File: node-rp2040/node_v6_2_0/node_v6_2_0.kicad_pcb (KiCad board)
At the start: 6 copper layers, 45 x 75 mm, 95 parts, among them J1 786463001, J10 Connector, USB-TYPE-C-16P, J11 Barrel_Jack_Switch, J2 U.FL, J3 Conn_Coaxial, J4 Conn_01x10, J5 Conn_01x10, J6 U.FL, J7 Barrel_Jack_Switch, J9 U.FL, Q1 DMG2301L, SW2 PTS636 SM50J SMTR LFS, SW3 PTS636 SM50J SMTR LFS, U1 RP2040, U12 CAT24M01W, U14 W25Q128, U2 USBLC6-2SC6, U3 AP2112K-3.3, U5 MCP73831-2-OT, U6 RFM69HCW, U7 PCF8523T, U8 SP3485EN, U9 SIM7080G, Y1 ABM8-272-T3

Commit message: finished layout v6.2
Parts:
- removed C8: 0.1u, JLCPCB:C_0402
- added C4: 0.1u, JLCPCB:C_0402, F.Cu at (125.2, 46.8)
- R17, R18: footprint JLCPCB:R_0805 -> JLCPCB:R_0603
- moved C48 145.5 mm to (106.6, 33.8), turned to 90 degrees
- moved C30 116.9 mm to (136.0, 50.8), turned to 180 degrees
- moved C47 108.0 mm to (109.1, 34.4)
- moved C9 106.4 mm to (127.5, 51.4)
- moved C25 104.3 mm to (127.5, 57.4)
- moved C44 102.8 mm to (112.9, 56.2)
- moved C17 102.0 mm to (134.9, 61.0), turned to 180 degrees
- moved R15 101.3 mm to (112.8, 53.6), turned to 180 degrees
- moved R4 98.8 mm to (113.2, 38.6), turned to -90 degrees
- moved R14 98.4 mm to (112.8, 54.6), turned to 180 degrees
- moved C28 98.2 mm to (138.2, 70.5), turned to 90 degrees
- moved R3 93.7 mm to (119.4, 29.0), turned to 90 degrees
- moved C13 92.6 mm to (110.8, 46.2), turned to 180 degrees
- moved C16 79.6 mm to (124.4, 58.0), turned to -90 degrees
- moved C15 79.0 mm to (122.2, 59.6), turned to -90 degrees
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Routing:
- net +3.3V: track 38.5 -> 57.8 mm, vias 0 -> 2
- net SDA: track 1.38 -> 15.1 mm, vias 1 -> 2
- net SCL: track 1.37 -> 14.2 mm, vias 1 -> 2
- net TX1: track 0.00 -> 12.4 mm
- net RX1: track 0.00 -> 11.5 mm
- net Net-(BT1-+): track 0.00 -> 10.9 mm
- net /MCU/CS: track 10.6 -> 1.39 mm
- net +1V1: track 9.45 -> 18.5 mm
- net /MCU/D1: track 9.96 -> 2.11 mm
- net /MCU/D3: track 15.3 -> 7.52 mm, vias 2 -> 1
- net /MCU/D0: track 14.3 -> 6.94 mm
- net USB-: track 0.00 -> 7.22 mm
- net /MCU/CLK: track 14.8 -> 8.09 mm, vias 2 -> 1
- net Net-(J10-CC1): track 0.00 -> 6.61 mm
- net 485_!RE: track 0.00 -> 6.55 mm, vias 0 -> 1
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
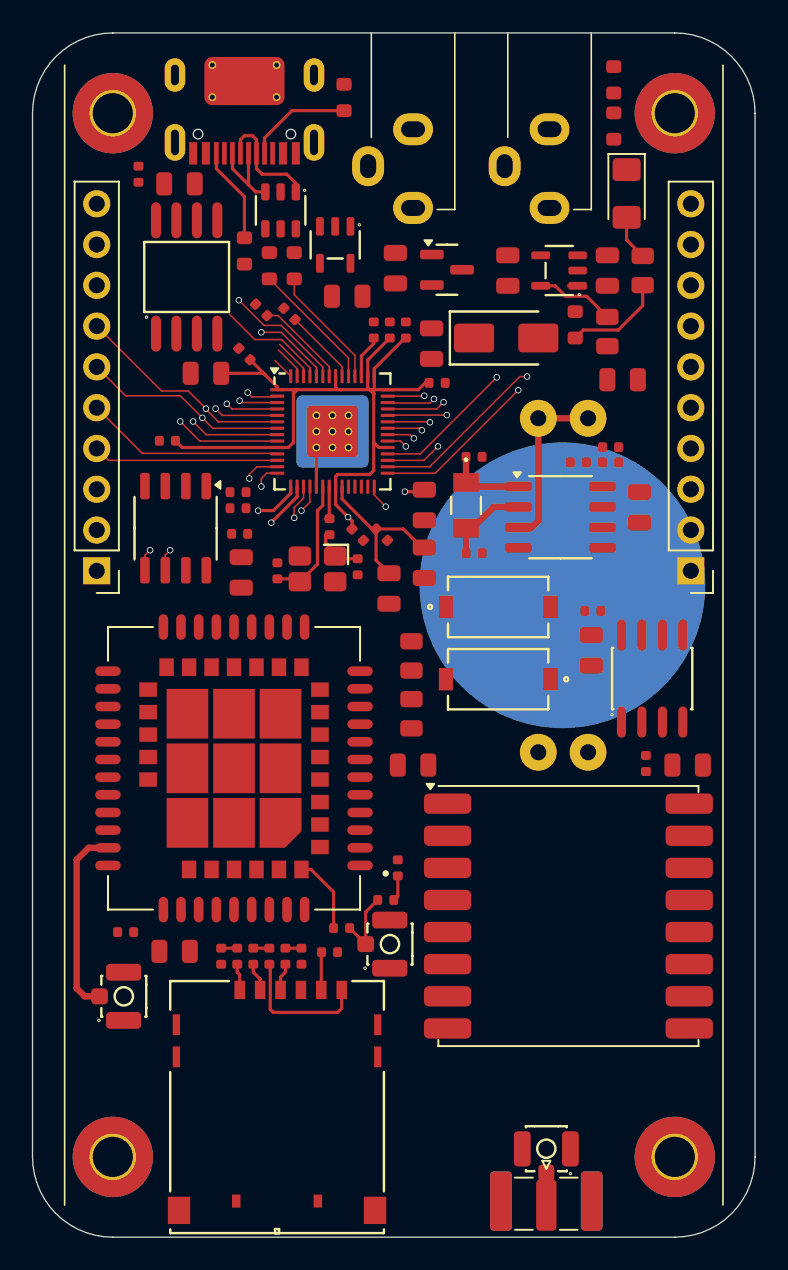
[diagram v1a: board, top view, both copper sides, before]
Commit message: finished routing; todo: labels and silkscreen, final review
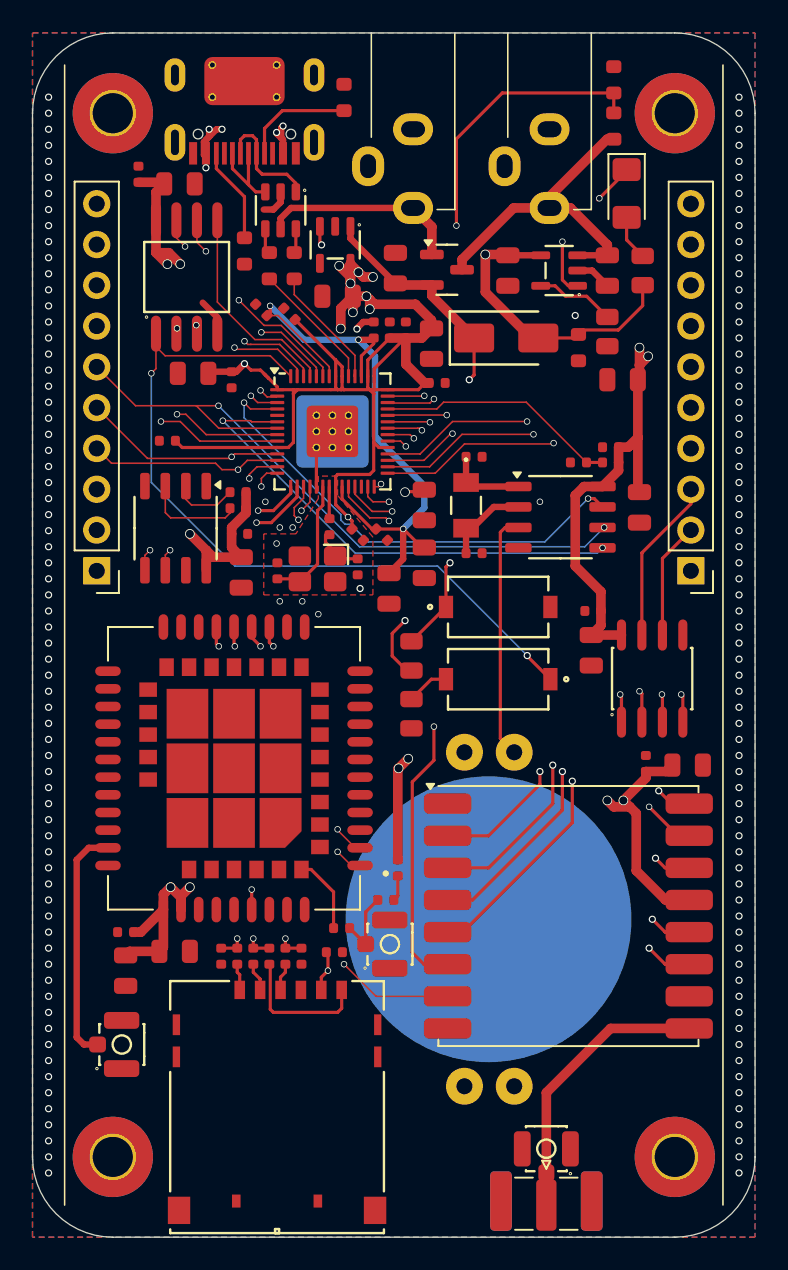
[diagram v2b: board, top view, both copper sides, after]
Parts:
- moved C42 22.0 mm to (105.8, 83.4), turned to -90 degrees
- moved BT1 21.3 mm to (128.4, 80.2)
- moved J6 3.00 mm to (104.8, 88.0)
- moved C5 1.79 mm to (112.4, 46.6), turned to -90 degrees
- moved R8 1.43 mm to (134.0, 44.6), turned to -90 degrees
- moved R14 1.00 mm to (112.8, 53.6)
- moved R15 1.00 mm to (112.8, 54.6)
- moved C13 0.80 mm to (110.0, 46.2)
- moved C40 0.60 mm to (119.0, 41.4)
- moved C37 0.30 mm to (118.8, 82.2)
- turned TH1 to 180 degrees
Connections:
- J6 pad 3: (no net) -> GND
- J9 pad 3: (no net) -> GND
- U1 pad 13: RFM_DIO0 -> RFM_DIO5
- U1 pad 14: RFM_DIO1 -> RFM_DIO3
- U1 pad 34: RFM_DIO2 -> RFM_DIO4
- U1 pad 35: RFM_DIO3 -> RFM_DIO0
- U1 pad 36: RFM_DIO4 -> RFM_DIO1
- U1 pad 37: RFM_DIO5 -> RFM_DIO2
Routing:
- net +3.3V: track 57.8 -> 295.6 mm, vias 2 -> 22
- net VBUS: track 6.31 -> 68.9 mm, vias 0 -> 6
- net MISO: track 0.00 -> 49.0 mm, vias 0 -> 3
- net /MCU/CS: track 1.39 -> 49.3 mm, vias 0 -> 2
- net 485_!RE: track 6.55 -> 50.6 mm, vias 1 -> 4
- net 485_DE: track 5.58 -> 49.3 mm, vias 1 -> 4
- net RFM_DIO3: track 1.73 -> 44.1 mm, vias 1 -> 4
- net SCL: track 14.2 -> 54.1 mm, vias 2 -> 3
- net RFM_DIO5: track 2.64 -> 42.2 mm, vias 1 -> 2
- net RFM_RST: track 3.49 -> 42.5 mm, vias 1 -> 2
- net RFM_DIO4: track 2.18 -> 39.9 mm, vias 1 -> 2
- net SDA: track 15.1 -> 52.2 mm, vias 2 -> 3
- net TX1: track 12.4 -> 49.3 mm, vias 0 -> 2
- net RFM_CS: track 1.54 -> 38.1 mm, vias 1 -> 2
- net +VSW: track 0.00 -> 35.3 mm, vias 0 -> 2
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- added copper zone on B.Cu, net GND
- added copper zone on F.Cu, net GND
- added copper zone on In1.Cu, net GND

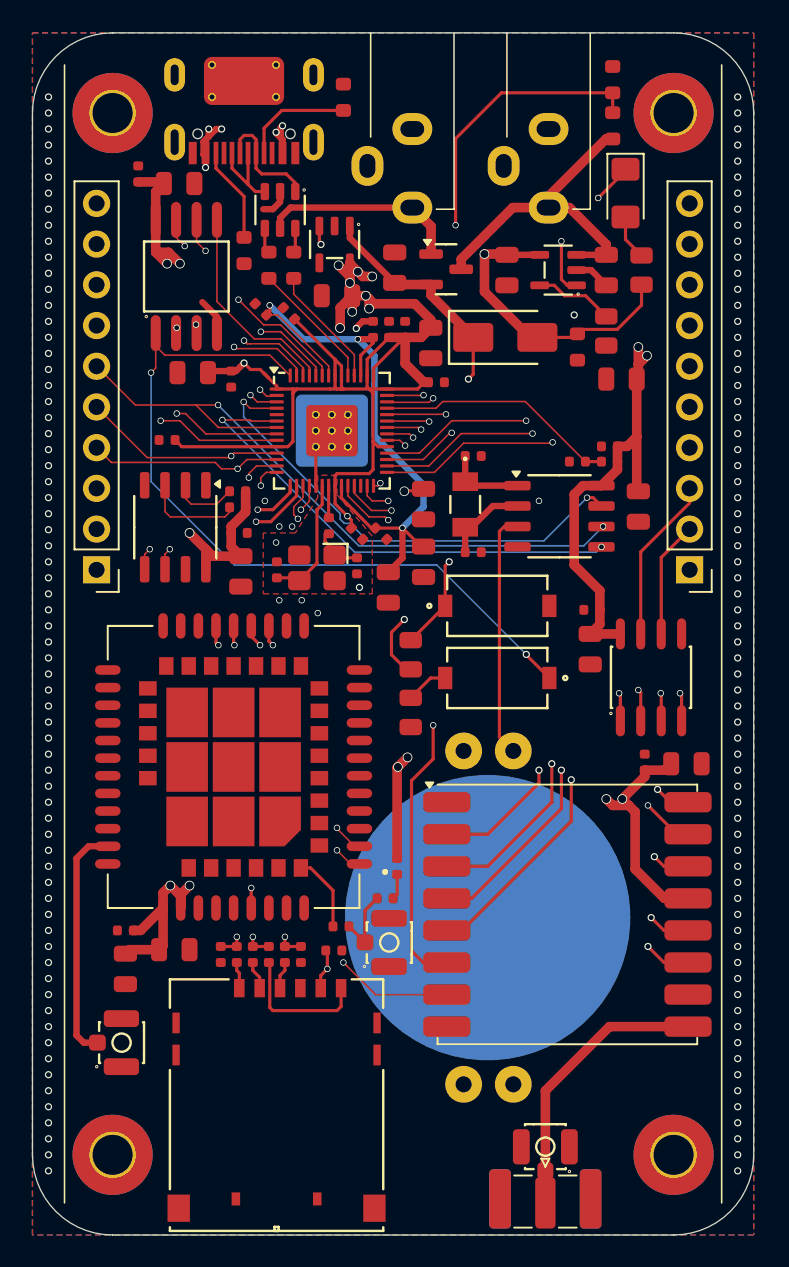
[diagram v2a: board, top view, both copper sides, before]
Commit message: added zener diode for overvoltage protection on vbus, small routing adjustments, silkscreen component labels
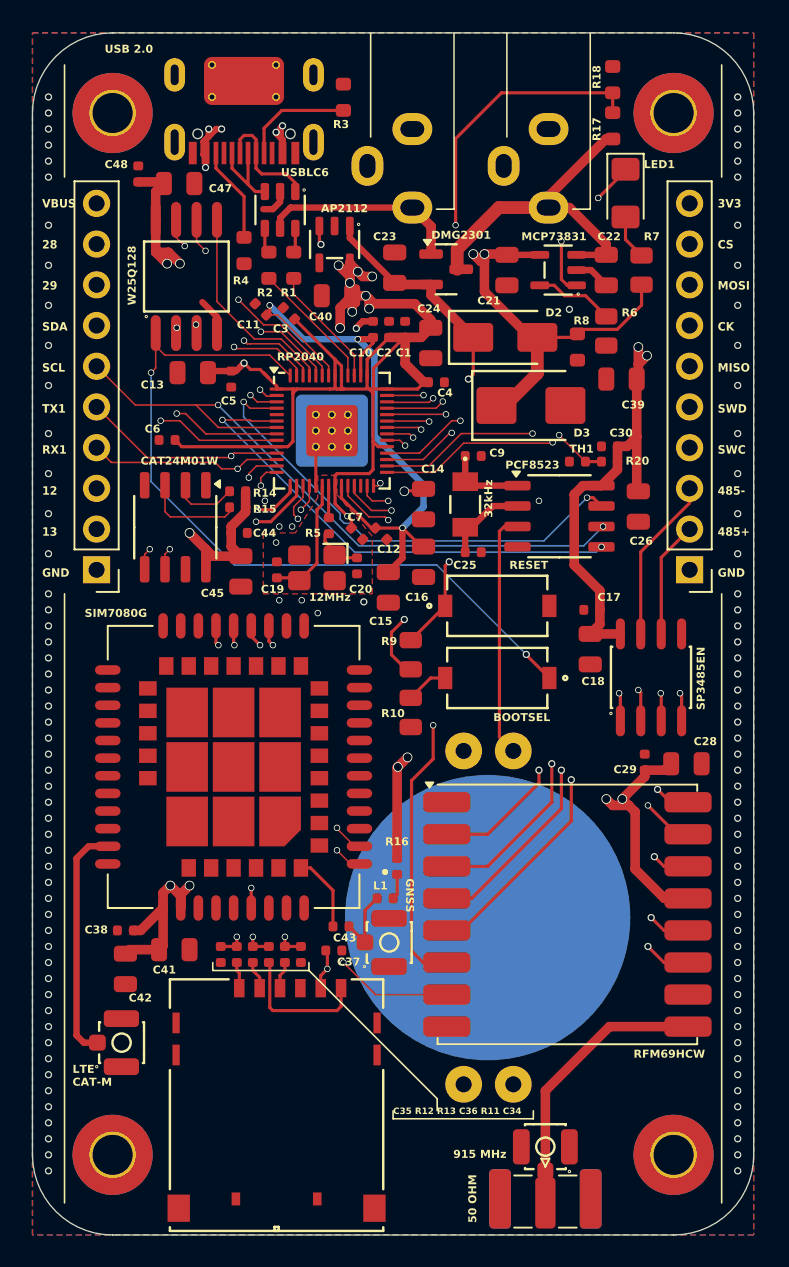
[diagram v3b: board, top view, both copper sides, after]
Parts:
- added D3: 1SMB5921BT3G, JLCPCB:D_SMB, F.Cu at (131.1, 48.2)
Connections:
- J6 pad 3: GND -> (no net)
- J9 pad 3: GND -> (no net)
- U1 pad 5: RTC_MFP2 -> unconnected-(U1-GPIO3-Pad5)
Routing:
- net VBUS: track 68.9 -> 75.4 mm, vias 6 -> 7
- net +BATT: track 20.7 -> 21.3 mm
- net RTC_TEMP: vias 0 -> 2
- net GND: vias 140 -> 108
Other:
- board text added: "12MHz"
- board text added: "32kHz"
- board text added: "3V3 CS MOSI CK MISO SWD SWC 485- 485+ GND"
- board text added: "50 OHM"
- board text added: "915 MHz"
- board text added: "AP2112"
- board text added: "BOOTSEL"
- board text added: "C10 C2 C1"
- board text added: "C11"
- board text added: "C12"
- board text added: "C13"
- board text added: "C14"
- board text added: "C15"
- board text added: "C16"
- board text added: "C17"
- board text added: "C18"
- board text added: "C19"
- board text added: "C20"
- board text added: "C21"
- board text added: "C22"
- board text added: "C23"
- board text added: "C24"
- board text added: "C25"
- board text added: "C26"
- board text added: "C28"
- board text added: "C29"
- board text added: "C3"
- board text added: "C30"
- board text added: "C35 R12 R13 C36 R11 C34"
- board text added: "C37"
- board text added: "C38"
- board text added: "C39"
- board text added: "C4"
- board text added: "C40"
- board text added: "C41"
- board text added: "C42"
- board text added: "C43"
- board text added: "C44"
- board text added: "C45"
- board text added: "C47"
- board text added: "C48"
- board text added: "C5"
- board text added: "C6"
- board text added: "C7"
- board text added: "C9"
- board text added: "CAT24M01W"
- board text added: "CR2032"
- board text added: "D2"
- board text added: "D3"
- board text added: "DMG2301"
- board text added: "GNSS"
- board text added: "L1"
- board text added: "LED1"
- board text added: "LTE CAT-M"
- board text added: "MCP73831"
- board text added: "PCF8523"
- board text added: "R10"
- board text added: "R14"
- board text added: "R15"
- board text added: "R16"
- board text added: "R17"
- board text added: "R18"
- board text added: "R2 R1"
- board text added: "R20"
- board text added: "R3"
- board text added: "R4"
- board text added: "R5"
- board text added: "R6"
- board text added: "R7"
- board text added: "R8"
- board text added: "R9"
- board text added: "RESET"
- board text added: "RFM69HCW"
- board text added: "RP2040"
- board text added: "SIM7080G"
- board text added: "SP3485EN"
- board text added: "TH1"
- board text added: "USB 2.0"
- board text added: "USBLC6"
- board text added: "VBUS 28 29 SDA SCL TX1 RX1 12 13 GND"
- board text added: "W25Q128"

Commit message: finish silkscreen and verification
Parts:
- added G***: LOGO, WiSDOM:wisdomcat, B.Cu at (106.6, 84.1)
- added G***: LOGO, logos:wisdom_logo_lineborder, B.Cu at (121.5, 63.2)
- added REF**: KiCad-Logo2_5mm_SilkScreen, Symbol:KiCad-Logo2_5mm_SilkScreen, B.Cu at (116.5, 95.0)
- added REF**: OSHW-Logo2_9.8x8mm_SilkScreen, Symbol:OSHW-Logo2_9.8x8mm_SilkScreen, B.Cu at (114.2, 87.8)
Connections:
- J2 pad 3: (no net) -> GND
- J6 pad 3: (no net) -> GND
- J9 pad 3: (no net) -> GND
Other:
- board text added: "3.7 V"
- board text added: "BAT"
- board text added: "BATTERY"
- board text added: "CHARGE"
- board text added: "LI-ION"
- board text added: "MAX 3 W"
- board text added: "MAX 6 V"
- board text added: "SMA"
- board text added: "U.FL"
- board text added: "VBUS"
- board text added: "VIN"
- board text added: "WiSDOM Node v6.2 Design by Amelia Vlahogiannis June 2025"
- board text added: "wisdomresearch.net"
- board text removed: "LED1"
